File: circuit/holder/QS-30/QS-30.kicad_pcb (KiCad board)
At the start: 2 copper layers, 20.8 x 20.6 mm, 2 parts, among them J1 Nixie_Conn_12P

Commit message: Update schematics
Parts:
- NX1: value QS27-1 -> QS30-1
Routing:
- net PA: track 17.0 -> 26.8 mm
- net P5: track 25.4 -> 17.0 mm
- net P9: track 12.1 -> 19.9 mm
- net P4: track 24.7 -> 18.6 mm

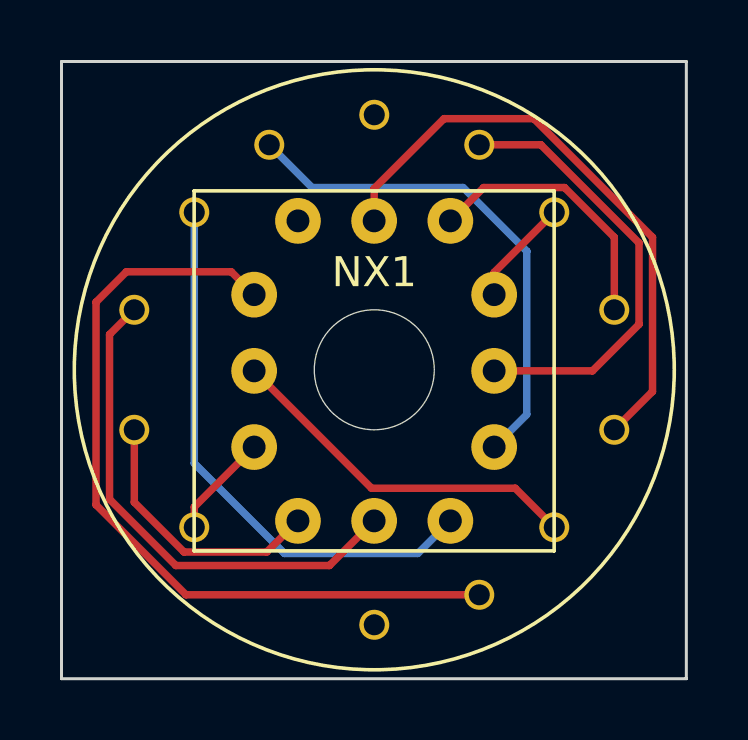
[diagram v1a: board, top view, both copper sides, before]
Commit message: Fix QS-30 layout
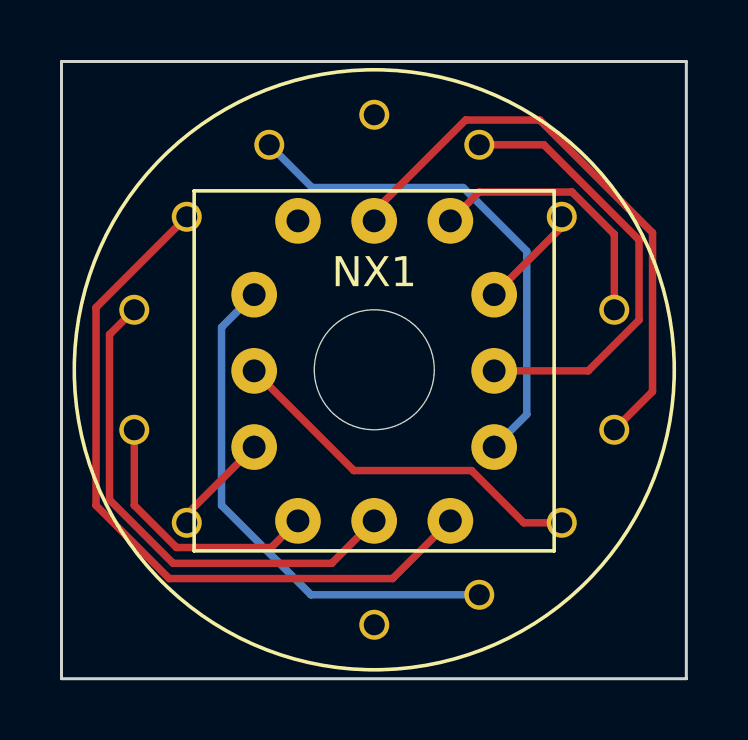
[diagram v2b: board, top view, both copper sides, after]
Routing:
- net PA: track 26.8 -> 17.3 mm
- net P4: track 18.6 -> 24.5 mm
